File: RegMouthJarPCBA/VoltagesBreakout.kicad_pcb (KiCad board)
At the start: 2 copper layers, 114.3 x 49.5 mm, 15 parts, among them J1 8P8C, P1 CONN_1, P2 CONN_1, P3 CONN_1, P4 CONN_1, P5 CONN_1, P6 CONN_1, P7 CONN_1, P8 CONN_1

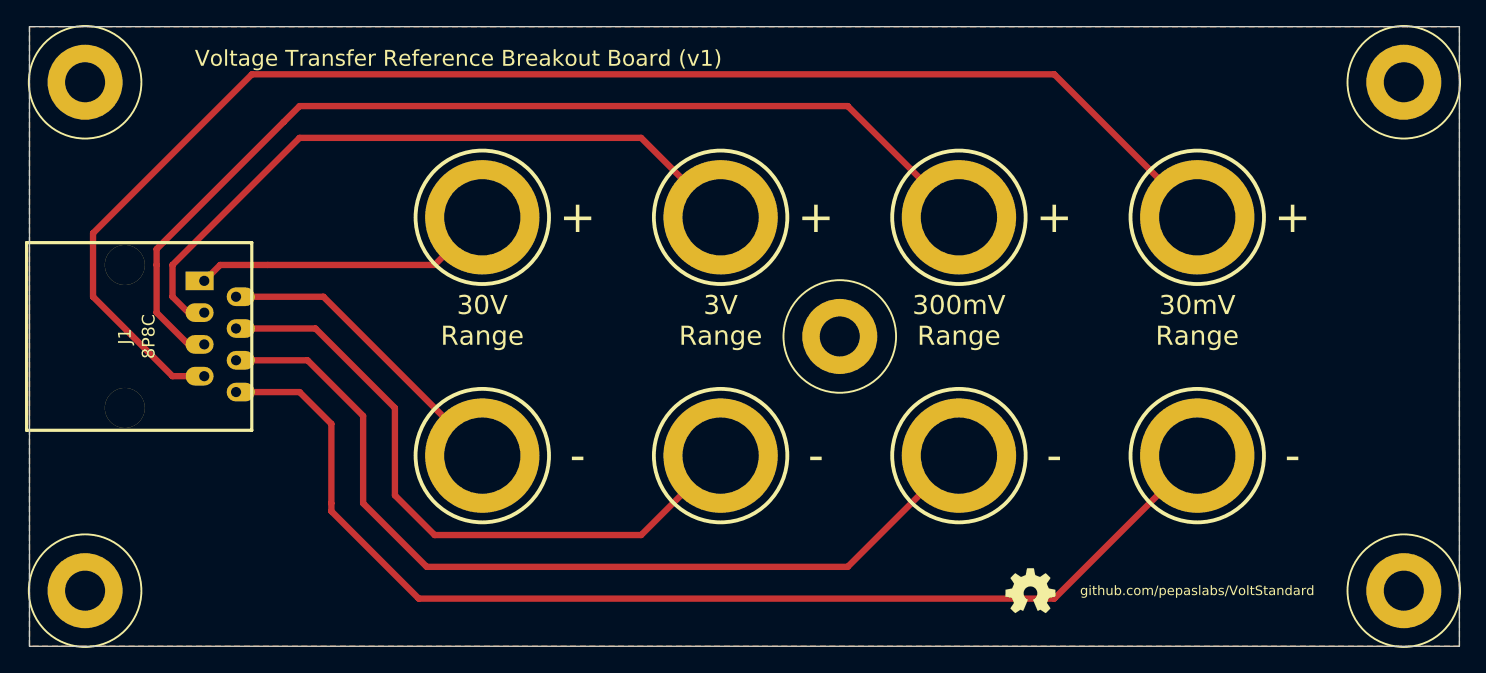
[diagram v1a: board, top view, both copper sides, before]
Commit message: updating voltage breakout board to fit within 10cm x 5cm for seeedstudio.
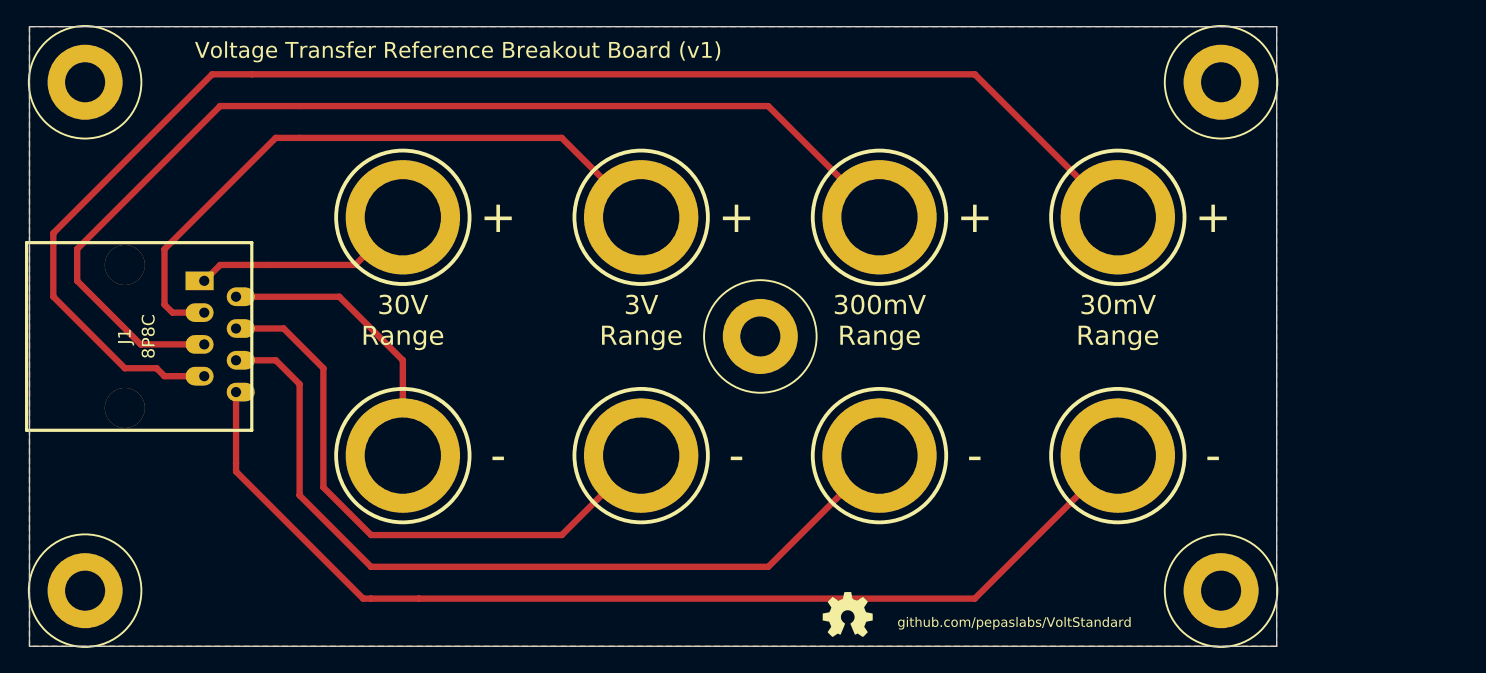
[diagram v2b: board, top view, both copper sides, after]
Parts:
- moved G*** 14.7 mm to (193.7, 153.7)
- moved H3 14.6 mm to (223.5, 111.1)
- moved H4 14.6 mm to (223.5, 151.8)
- moved P7 6.35 mm to (215.3, 121.9)
- moved P8 6.35 mm to (215.3, 141.0)
- moved H*** 6.35 mm to (186.7, 131.4)
- moved P1 6.35 mm to (158.1, 121.9)
- moved P2 6.35 mm to (158.1, 141.0)
- moved P3 6.35 mm to (177.2, 121.9)
- moved P4 6.35 mm to (177.2, 141.0)
- moved P5 6.35 mm to (196.2, 121.9)
- moved P6 6.35 mm to (196.2, 141.0)
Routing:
- net N-000007: track 92.5 -> 85.8 mm
- net N-0000012: track 24.3 -> 18.0 mm
- net N-000001: track 72.4 -> 67.2 mm
- net N-000005: track 82.5 -> 87.4 mm
- net N-000004: track 52.3 -> 47.4 mm
- net N-000003: track 56.3 -> 52.3 mm
- net N-000002: track 24.9 -> 23.1 mm
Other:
- board size 114.3 x 49.5 mm -> 99.7 x 49.5 mm
